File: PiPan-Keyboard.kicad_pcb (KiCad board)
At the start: 2 copper layers, 260.3 x 76.2 mm, 101 parts, among them J0 Conn_01x18_MountingPin, SW0 RotaryEncoder_Switch, U1 Pico

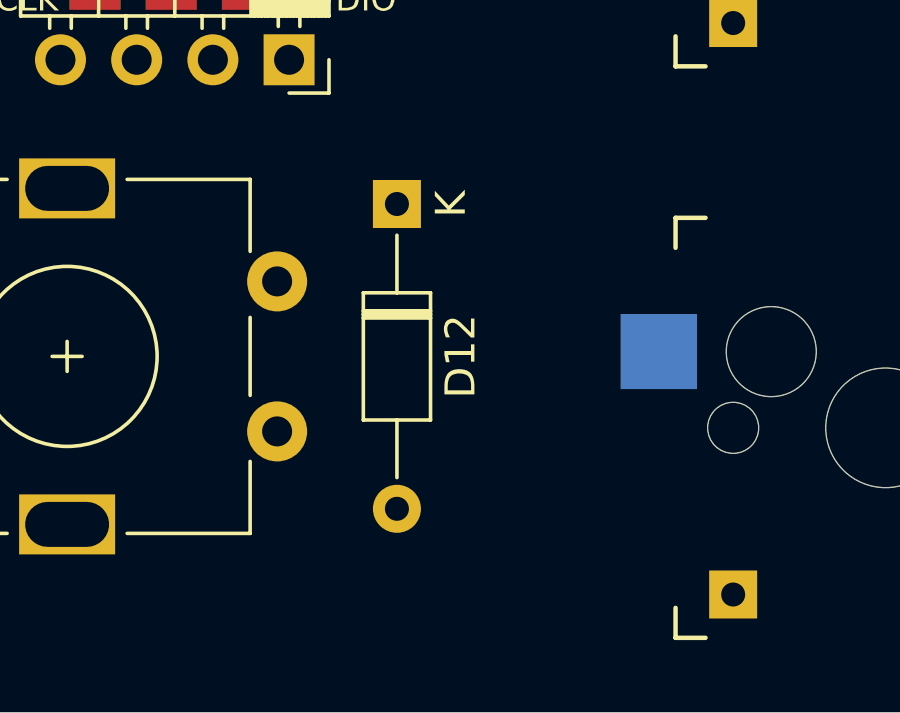
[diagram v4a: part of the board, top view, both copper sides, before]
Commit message: moved encoder diode
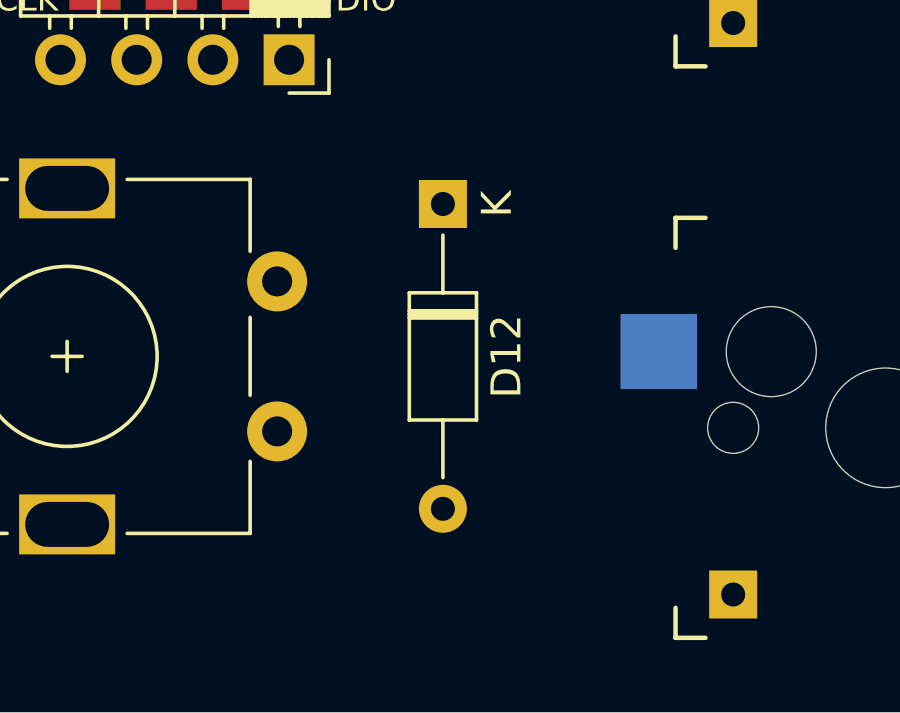
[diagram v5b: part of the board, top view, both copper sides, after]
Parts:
- moved D12 1.53 mm to (53.5, 120.3)
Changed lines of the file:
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@@
   )
   (footprint "Diode_THT:D_DO-35_SOD27_P10.16mm_Horizontal" (layer "F.Cu")
-    (at 51.975 120.3325 -90)
+    (at 53.5075 120.3325 -90)
     (descr "Diode, DO-35_SOD27 series, Axial, Horizontal, pin pitch=10.16mm, , length*diameter=4*2mm^2, , http://www.diodes.com/_files/packages/DO-35.pdf")
     (tags "Diode DO-35_SOD27 series Axial Horizontal pin pitch 10.16mm  length 4mm diameter 2mm")

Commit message: expanded left edge of pcb, generated new .step
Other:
- board size 260.3 x 76.2 mm -> 261.1 x 76.2 mm
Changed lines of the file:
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@@
     )
   )
-  (gr_arc (start 27.78125 137.31875) (mid 27.220013 137.086237) (end 26.9875 136.525) (layer "Edge.Cuts") (width 0.1))
-  (gr_arc (start 26.9875 61.9125) (mid 27.219984 61.351234) (end 27.78125 61.11875) (layer "Edge.Cuts") (width 0.1))
-  (gr_line (start 27.78125 61.11875) (end 286.54375 61.11875) (layer "Edge.Cuts") (width 0.1))
-  (gr_line (start 26.9875 136.525) (end 26.9875 61.9125) (layer "Edge.Cuts") (width 0.1))
+  (gr_arc (start 26.9875 137.31875) (mid 26.426263 137.086237) (end 26.19375 136.525) (layer "Edge.Cuts") (width 0.1))
+  (gr_arc (start 26.19375 61.9125) (mid 26.426234 61.351234) (end 26.9875 61.11875) (layer "Edge.Cuts") (width 0.1))
+  (gr_line (start 26.19375 136.525) (end 26.19375 61.9125) (layer "Edge.Cuts") (width 0.1))
   (gr_line (start 287.3375 136.525) (end 287.3375 61.9125) (layer "Edge.Cuts") (width 0.1))
-  (gr_line (start 286.54375 137.31875) (end 27.78125 137.31875) (layer "Edge.Cuts") (width 0.1))
+  (gr_line (start 26.9875 61.11875) (end 286.54375 61.11875) (layer "Edge.Cuts") (width 0.1))
   (gr_arc (start 286.54375 61.11875) (mid 287.105016 61.351234) (end 287.3375 61.9125) (layer "Edge.Cuts") (width 0.1))
   (gr_arc (start 287.3375 136.525) (mid 287.104998 137.086234) (end 286.54375 137.31875) (layer "Edge.Cuts") (width 0.1))
+  (gr_line (start 26.9875 137.31875) (end 286.54375 137.31875) (layer "Edge.Cuts") (width 0.1))
 )
